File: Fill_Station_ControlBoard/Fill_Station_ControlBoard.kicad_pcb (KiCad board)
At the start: 4 copper layers, 161 parts, among them J10 Screw_Terminal_2_P5.00mm, J3 USB_C_Receptacle_USB2.0_14P, J4 Conn_02x05_Counter_Clockwise, J5 436500200, J6 RJ45_Wuerth_7499010211A, J7 436500200, J8 DE9_Socket_MountingHoles, J9 436500200, SW1 CK_KMS2xxG, U1 STM32H747IITx, U2 USBLC6-2SC6, U3 TCAN337G, U4 TPS2116DRL, U5 LAN8742A, U7 OKI-78SR-5_1.5-W36-C, Y1 ASV-32.768kHz, Y1 Crystal 25MHz, Y2 Crystal 32.768 kHz, Y3 ASV-25.000MHz

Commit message: début layout
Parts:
- removed the C26 at (128.3, 82.5)
- removed the C27 at (128.3, 85.0)
- removed the C33 at (130.6, 72.5)
- removed the C34 at (130.6, 75.0)
- removed C79, C80, C81, C82, C84, C85: C, Capacitor_SMD:C_0603_1608Metric
- removed R89, R90: R_US, Resistor_SMD:R_0603_1608Metric
- removed the Y1 at (134.4, 84.4)
- removed the Y2 at (136.1, 73.8)
- added C10: 47uF, Capacitor_SMD:CP_Elec_4x5.4, F.Cu at (269.0, 162.6)
- added C11: 47uF, Capacitor_SMD:CP_Elec_4x5.4, F.Cu at (281.8, 162.7)
- added C5: 10u, Capacitor_SMD:C_0603_1608Metric, F.Cu at (223.8, 190.7)
- added C55: 10u, Capacitor_SMD:C_0603_1608Metric, F.Cu at (242.5, 125.3)
- added C56: 0.1u, Capacitor_SMD:C_0603_1608Metric, F.Cu at (242.5, 127.8)
- added C58: 3.3n, Capacitor_SMD:C_0603_1608Metric, F.Cu at (242.5, 130.3)
- added C8: 100n, Capacitor_SMD:C_0603_1608Metric, F.Cu at (223.8, 188.1)
- added CR1: ESDCAN02-2BWY, ESDCAN:SOT323-3L_STM, B.Cu at (185.1, 151.5)
- added D15: 6.4V, Diode_SMD:D_0603_1608Metric, F.Cu at (248.5, 120.0)
- added D4: LED, LED_SMD:LED_0603_1608Metric, F.Cu at (269.0, 156.2)
- added D5: LED, LED_SMD:LED_0603_1608Metric, F.Cu at (285.5, 158.9)
- added F1: Fuse, Fuse:Fuse_0603_1608Metric, F.Cu at (247.1, 165.8)
- added F2: Polyfuse, Fuse:Fuse_0603_1608Metric, F.Cu at (248.5, 122.5)
- added IC1: TPS259573DSGR, Package_SON:WSON-8-1EP_2x2mm_P0.5mm_EP0.9x1.6mm_ThermalVias, F.Cu at (247.2, 157.1)
- added J10: Screw_Terminal_6_P5.00mm, TerminalBlock_Phoenix:TerminalBlock_Phoenix_PT-1,5-6-5.0-H_1x06_P5.00mm_Horizontal, F.Cu at (122.6, 106.8)
- added J11: Micro_SD_Card_Det1, Connector_Card:microSD_HC_Molex_47219-2001, F.Cu at (293.6, 104.7)
- added J2: Ematch1, TerminalBlock_Phoenix:TerminalBlock_Phoenix_PT-1,5-2-5.0-H_1x02_P5.00mm_Horizontal, F.Cu at (270.9, 172.7)
- added J6: Ematch2, TerminalBlock_Phoenix:TerminalBlock_Phoenix_PT-1,5-2-5.0-H_1x02_P5.00mm_Horizontal, F.Cu at (282.5, 172.7)
- added J7: Screw_Terminal_3_P5.00mm, TerminalBlock_Phoenix:TerminalBlock_Phoenix_PT-1,5-3-5.0-H_1x03_P5.00mm_Horizontal, F.Cu at (122.6, 139.1)
- added J8: Screw_Terminal_3_P5.00mm, TerminalBlock_Phoenix:TerminalBlock_Phoenix_PT-1,5-3-5.0-H_1x03_P5.00mm_Horizontal, F.Cu at (132.7, 146.7)
- added J9: Screw_Terminal_3_P5.00mm, TerminalBlock_Phoenix:TerminalBlock_Phoenix_PT-1,5-3-5.0-H_1x03_P5.00mm_Horizontal, F.Cu at (150.0, 146.7)
- added Q1: AO3400A, Package_TO_SOT_SMD:SOT-23, F.Cu at (275.7, 162.6)
- added Q2: AO3400A, Package_TO_SOT_SMD:SOT-23, F.Cu at (288.5, 162.7)
- added R14: 10k, Resistor_SMD:R_0603_1608Metric_Pad0.98x0.95mm_HandSolder, F.Cu at (219.6, 198.2)
- added R16: 10k, Resistor_SMD:R_0603_1608Metric_Pad0.98x0.95mm_HandSolder, F.Cu at (219.6, 195.7)
- added R18: 49.9, Resistor_SMD:R_0603_1608Metric_Pad0.98x0.95mm_HandSolder, F.Cu at (219.6, 188.1)
- added R20: 49.9, Resistor_SMD:R_0603_1608Metric_Pad0.98x0.95mm_HandSolder, F.Cu at (219.6, 190.7)
- added R21: 49.9, Resistor_SMD:R_0603_1608Metric_Pad0.98x0.95mm_HandSolder, F.Cu at (219.6, 193.2)
- added R22: 49.9, Resistor_SMD:R_0603_1608Metric_Pad0.98x0.95mm_HandSolder, F.Cu at (219.6, 200.7)
- added R25: 22, Resistor_SMD:R_0603_1608Metric_Pad0.98x0.95mm_HandSolder, F.Cu at (297.2, 162.6)
- added R26: 10k, Resistor_SMD:R_0603_1608Metric_Pad0.98x0.95mm_HandSolder, F.Cu at (297.2, 152.5)
- added R27: 50k, Resistor_SMD:R_0603_1608Metric_Pad0.98x0.95mm_HandSolder, F.Cu at (297.2, 157.5)
- added R28: 10k, Resistor_SMD:R_0603_1608Metric_Pad0.98x0.95mm_HandSolder, F.Cu at (297.2, 155.0)
- added R31: *, Resistor_SMD:R_0603_1608Metric_Pad0.98x0.95mm_HandSolder, F.Cu at (297.2, 160.1)
- added R33: *, Resistor_SMD:R_0603_1608Metric_Pad0.98x0.95mm_HandSolder, F.Cu at (297.2, 175.1)
- added R34: 22, Resistor_SMD:R_0603_1608Metric_Pad0.98x0.95mm_HandSolder, F.Cu at (297.2, 165.1)
- added R35: 10k, Resistor_SMD:R_0603_1608Metric_Pad0.98x0.95mm_HandSolder, F.Cu at (297.2, 167.6)
- added R36: 50k, Resistor_SMD:R_0603_1608Metric_Pad0.98x0.95mm_HandSolder, F.Cu at (297.2, 170.1)
- added R37: 10k, Resistor_SMD:R_0603_1608Metric_Pad0.98x0.95mm_HandSolder, F.Cu at (297.2, 172.6)
- added R38: 22, Resistor_SMD:R_0402_1005Metric, F.Cu at (225.8, 79.9)
- added R39: 22, Resistor_SMD:R_0402_1005Metric, F.Cu at (235.7, 89.6)
- added R40: 22, Resistor_SMD:R_0402_1005Metric, F.Cu at (224.8, 79.9)
- added R41: 22, Resistor_SMD:R_0402_1005Metric, F.Cu at (223.8, 79.9)
- added R42: 22, Resistor_SMD:R_0402_1005Metric, F.Cu at (235.7, 88.6)
- added R43: 10k, Resistor_SMD:R_0402_1005Metric, F.Cu at (275.5, 98.9)
- added R44: 10k, Resistor_SMD:R_0402_1005Metric, F.Cu at (276.7, 98.9)
- added R45: 10k, Resistor_SMD:R_0402_1005Metric, F.Cu at (277.9, 98.9)
- added R46: 10k, Resistor_SMD:R_0402_1005Metric, F.Cu at (279.1, 98.9)
- added R47: 10k, Resistor_SMD:R_0402_1005Metric, F.Cu at (280.3, 98.9)
- added R48: 10k, Resistor_SMD:R_0402_1005Metric, F.Cu at (281.4, 98.9)
- added R59: 100k, Resistor_SMD:R_0805_2012Metric, F.Cu at (238.3, 125.5)
- added R60: *, Resistor_SMD:R_0805_2012Metric, F.Cu at (238.3, 128.4)
- added R61: *, Resistor_SMD:R_0805_2012Metric, F.Cu at (238.3, 131.4)
- added U4: TPS62130, Package_DFN_QFN:VQFN-16-1EP_3x3mm_P0.5mm_EP1.68x1.68mm_ThermalVias, F.Cu at (239.1, 121.3)
- C6: renamed from C28; value ~ -> 10u
- C60: renamed from C37; moved to B.Cu
- C61: renamed from C83; value C -> 22u
- C62: renamed from C38; moved to B.Cu
- C7: renamed from C29; value ~ -> 100n
- R1: renamed from R24; value 33 -> 22
- R17: renamed from R37; value 270 -> 10k
- R2: value 33 -> 22
- R3: renamed from R36; value 33 -> 22
- R4: renamed from R21; value 33 -> 22
- R52: renamed from R38; footprint Resistor_SMD:R_0603_1608Metric_Pad0.98x0.95mm_HandSolder -> Capacitor_SMD:C_0402_1005Metric
- R54: renamed from R47; footprint Resistor_SMD:R_0603_1608Metric_Pad0.98x0.95mm_HandSolder -> Capacitor_SMD:C_0402_1005Metric
- R6: renamed from R22; value 33 -> 22
- R65: renamed from R15; footprint Resistor_SMD:R_0805_2012Metric -> Capacitor_SMD:C_0603_1608Metric
- R66: renamed from R16; footprint Resistor_SMD:R_0805_2012Metric -> Capacitor_SMD:C_0603_1608Metric
- R7: renamed from R25; value 33 -> 22
- R75: renamed from R29; footprint Resistor_SMD:R_0805_2012Metric -> Capacitor_SMD:C_0603_1608Metric
- R8: renamed from R23; value 33 -> 22
- moved C64 341.9 mm to (245.1, 157.1), turned to 90 degrees
- moved U3 338.5 mm to (255.0, 148.8), turned to 90 degrees
- moved C57 336.2 mm to (253.3, 172.3)
- moved R78 335.2 mm to (248.4, 153.8)
- moved R67 333.7 mm to (243.3, 160.1), turned to 180 degrees
- moved R77 333.2 mm to (245.1, 153.5), turned to 90 degrees
- moved R73 331.8 mm to (252.1, 157.1), turned to 90 degrees
- moved R68 330.9 mm to (242.6, 157.8), turned to 90 degrees
- moved C59 329.6 mm to (253.4, 164.2)
- moved C61 329.0 mm to (247.5, 130.4)
- moved C12 328.3 mm to (278.7, 106.1)
- moved C13 328.3 mm to (278.7, 108.6)
- moved D6 327.7 mm to (240.0, 164.5), turned to 180 degrees
- moved J13 325.6 mm to (242.1, 172.4)
- moved R66 317.1 mm to (259.1, 136.2), turned to 90 degrees
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- renumbered C12 to C1, C45 to C12, C46 to C13, C6 to C15, C48 to C16, C31 to C17, C25 to C18, C24 to C19, C9 to C2, C32 to C20, C23 to C21, C42 to C22, C43 to C23, C44 to C24, C55 to C25, C2 to C26, C3 to C27, C56 to C28, C4 to C29, C10 to C3, C1 to C30, C5 to C31, C19 to C32, C8 to C33, C20 to C34, C14 to C35, C57 to C36, C15 to C37, C21 to C38, C16 to C39, C13 to C4, C22 to C40, C17 to C41, C36 to C42, C18 to C43, C54 to C44, C50 to C45, C7 to C46, C49 to C47, C33 to C48, C26 to C49, C11 to C50, C27 to C51, C34 to C52, C40 to C53, C41 to C54, C52 to C57, C53 to C59, C60 to C64, C35 to C66, C51 to C9, D12 to D1, D6 to D10, D5 to D11, D7 to D12, D8 to D13, D9 to D14, D11 to D2, D10 to D3, D13 to D6, D2 to D7, D4 to D8, D1 to D9, J6 to J1, J4 to J12, J10 to J13, J8 to J14, J3 to J15, J7 to J3, J9 to J4, R32 to R10, R33 to R11, R26 to R12, R17 to R13, R30 to R15, R8 to R19, R18 to R23, R19 to R24, R1 to R29, R9 to R30, R20 to R32, R27 to R49, R28 to R5, R14 to R50, R39 to R51, R48 to R53, R42 to R55, R43 to R56, R46 to R57, R5 to R58, R44 to R62, R53 to R63, R54 to R64, R51 to R67, R52 to R68, R34 to R69, R35 to R70, R55 to R71, R40 to R72, R69 to R73, R41 to R74, R45 to R76, R67 to R77, R68 to R78, R3 to R79, R4 to R80, R13 to R81, R12 to R82, R31 to R9, U5 to U1, U1 to U2, U7 to U3, U3 to U5, U4 to U6, U2 to U7, Y3 to Y1, Y1 to Y2
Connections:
- net Net-(J3-D+-PadA6) renamed /USB/D+
- net Net-(J3-D--PadA7) renamed /USB/D-
- net Net-(J5-Pad1) renamed /Control/Servo1
- net Net-(J7-Pad1) renamed /Control/Servo2
- net Net-(J9-Pad1) renamed /Control/Servo3
- C6 pad 1: Net-(U5-VDD1A) -> 3V3A
- C7 pad 1: Net-(U5-VDD1A) -> 3V3A
- C9 pad 1: 3V3 -> 3V3A
- J1 pad 4: 3V3 -> 3V3A
- J1 pad 5: 3V3 -> 3V3A
- J1 pad 8: CHASSIS -> unconnected-(J1-Pad8)
- U1 pad 1: Net-(U5-VDD1A) -> 3V3A
- U1 pad 19: Net-(U5-VDD1A) -> 3V3A
- U1 pad 5: unconnected-(U5-XTAL1/CLKIN-Pad5) -> /MCU/Clock_25Mhz
- U6 pad 5: unconnected-(U4-MODE-Pad5) -> 5V_BAT
- U7 pad 5: +5V -> 5V_USB
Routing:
- net /CAN FD/CAN_P: track 0.00 -> 20.7 mm, vias 0 -> 1
- net /CAN FD/CAN_N: track 0.00 -> 16.2 mm, vias 0 -> 1
- net GND: track 0.00 -> 13.5 mm, vias 0 -> 7
- net Net-(IC1-~{EN}/OVLO): track 0.00 -> 6.33 mm
- net Net-(F1-Pad1): track 0.00 -> 5.81 mm
- net 3V3: track 0.00 -> 4.59 mm, vias 0 -> 1
- net Net-(U5-S): track 0.00 -> 3.57 mm
- net Net-(U5-RXD): track 0.00 -> 3.38 mm
- net Net-(U5-TXD): track 0.00 -> 3.38 mm
- net Net-(U6-PR1): track 0.00 -> 3.36 mm
- net Net-(IC1-ILM): track 0.00 -> 2.86 mm
- net 5V: track 0.00 -> 2.55 mm
- net 5V_BAT: track 0.00 -> 2.49 mm
- net /CAN FD/CAN.FAULT: track 0.00 -> 2.24 mm
- net Net-(U6-ST): track 0.00 -> 2.15 mm
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- added copper zone on F.Cu, net 12.8V
- added copper zone on F.Cu, net 12.8V_BAT
- added copper zone on In2.Cu, net 3V3
- added copper zone on F.Cu, net 5V
- added copper zone on F.Cu, net 5V_BAT
- added copper zone on F.Cu, net 5V_USB
- added copper zone on In1.Cu, net GND

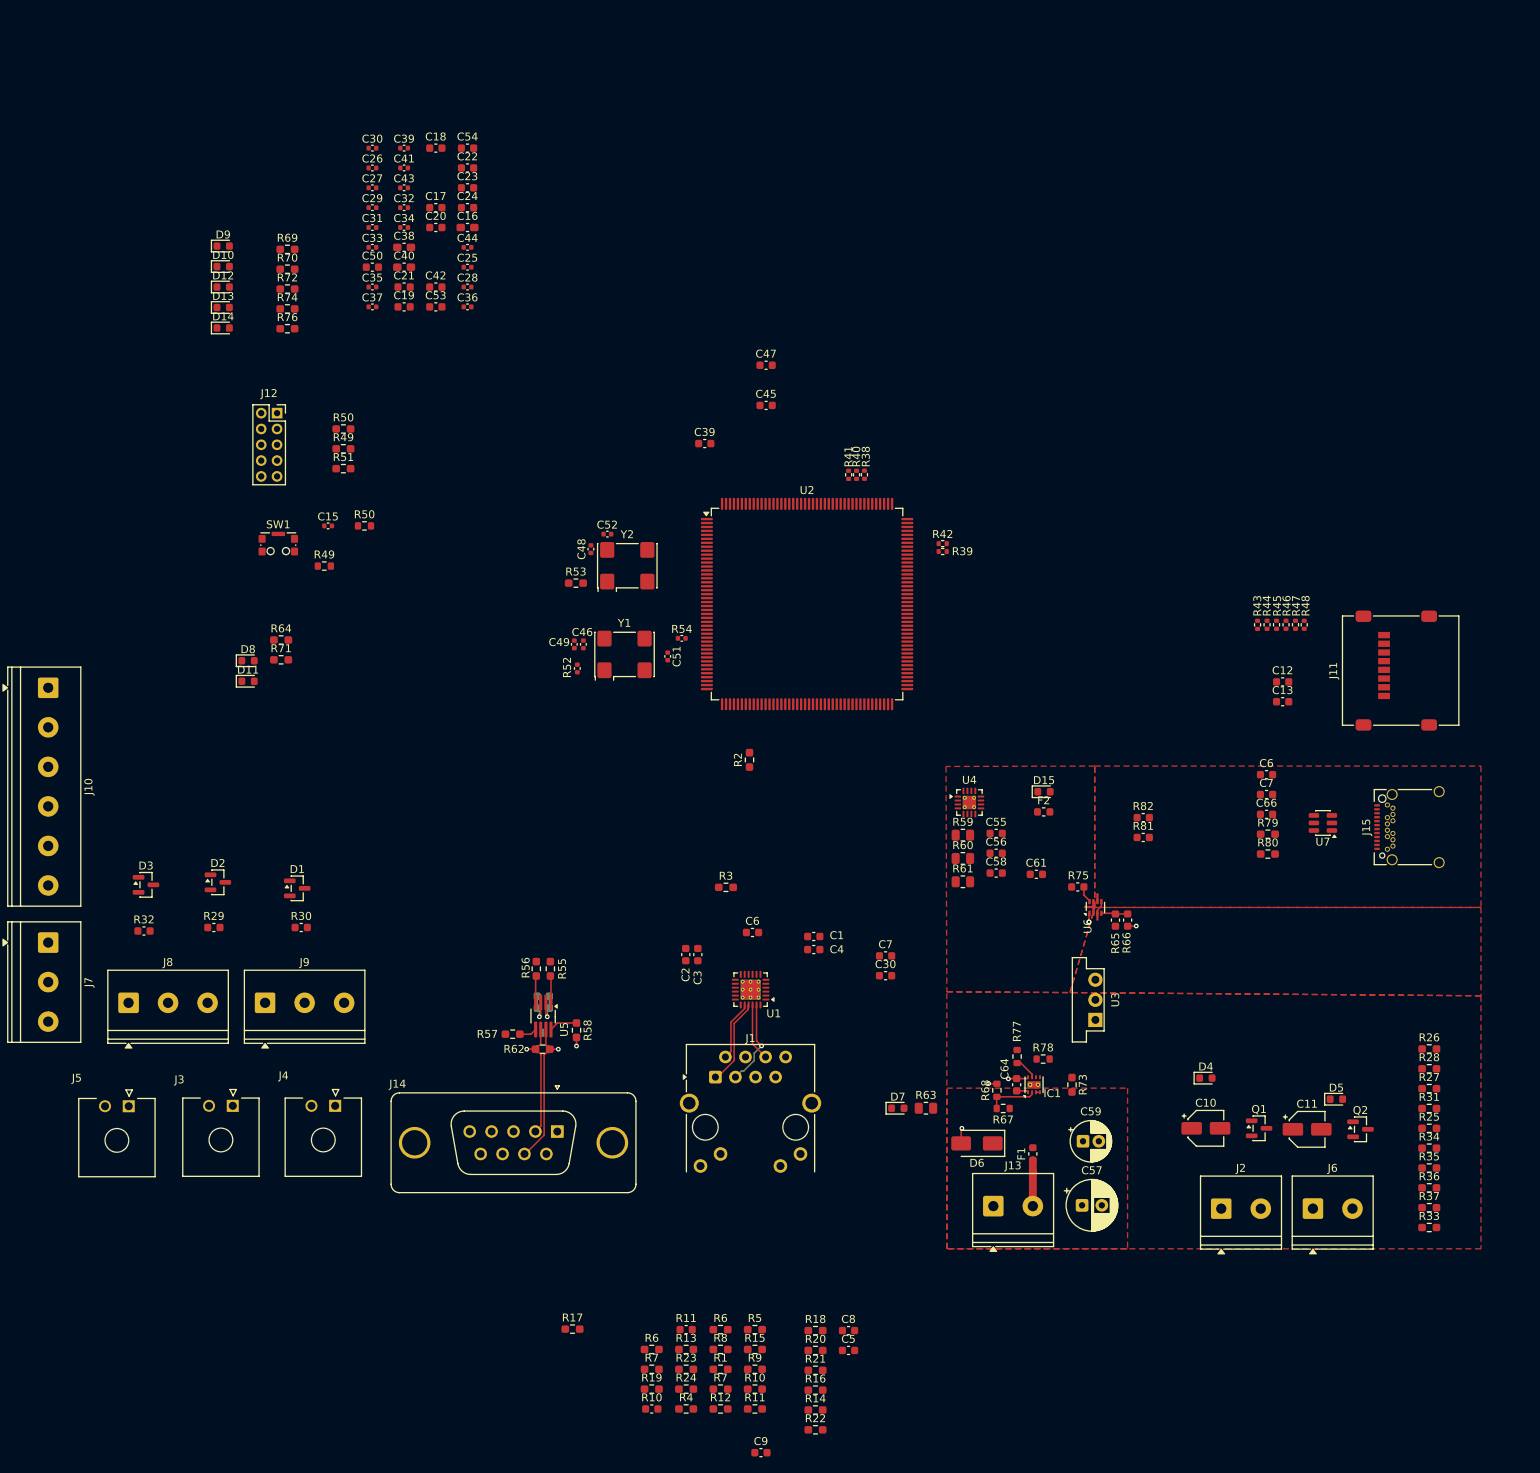
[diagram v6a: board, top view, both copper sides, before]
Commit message: wiring de certaines parties du PCB et placement de quelques composantes sur le PCB
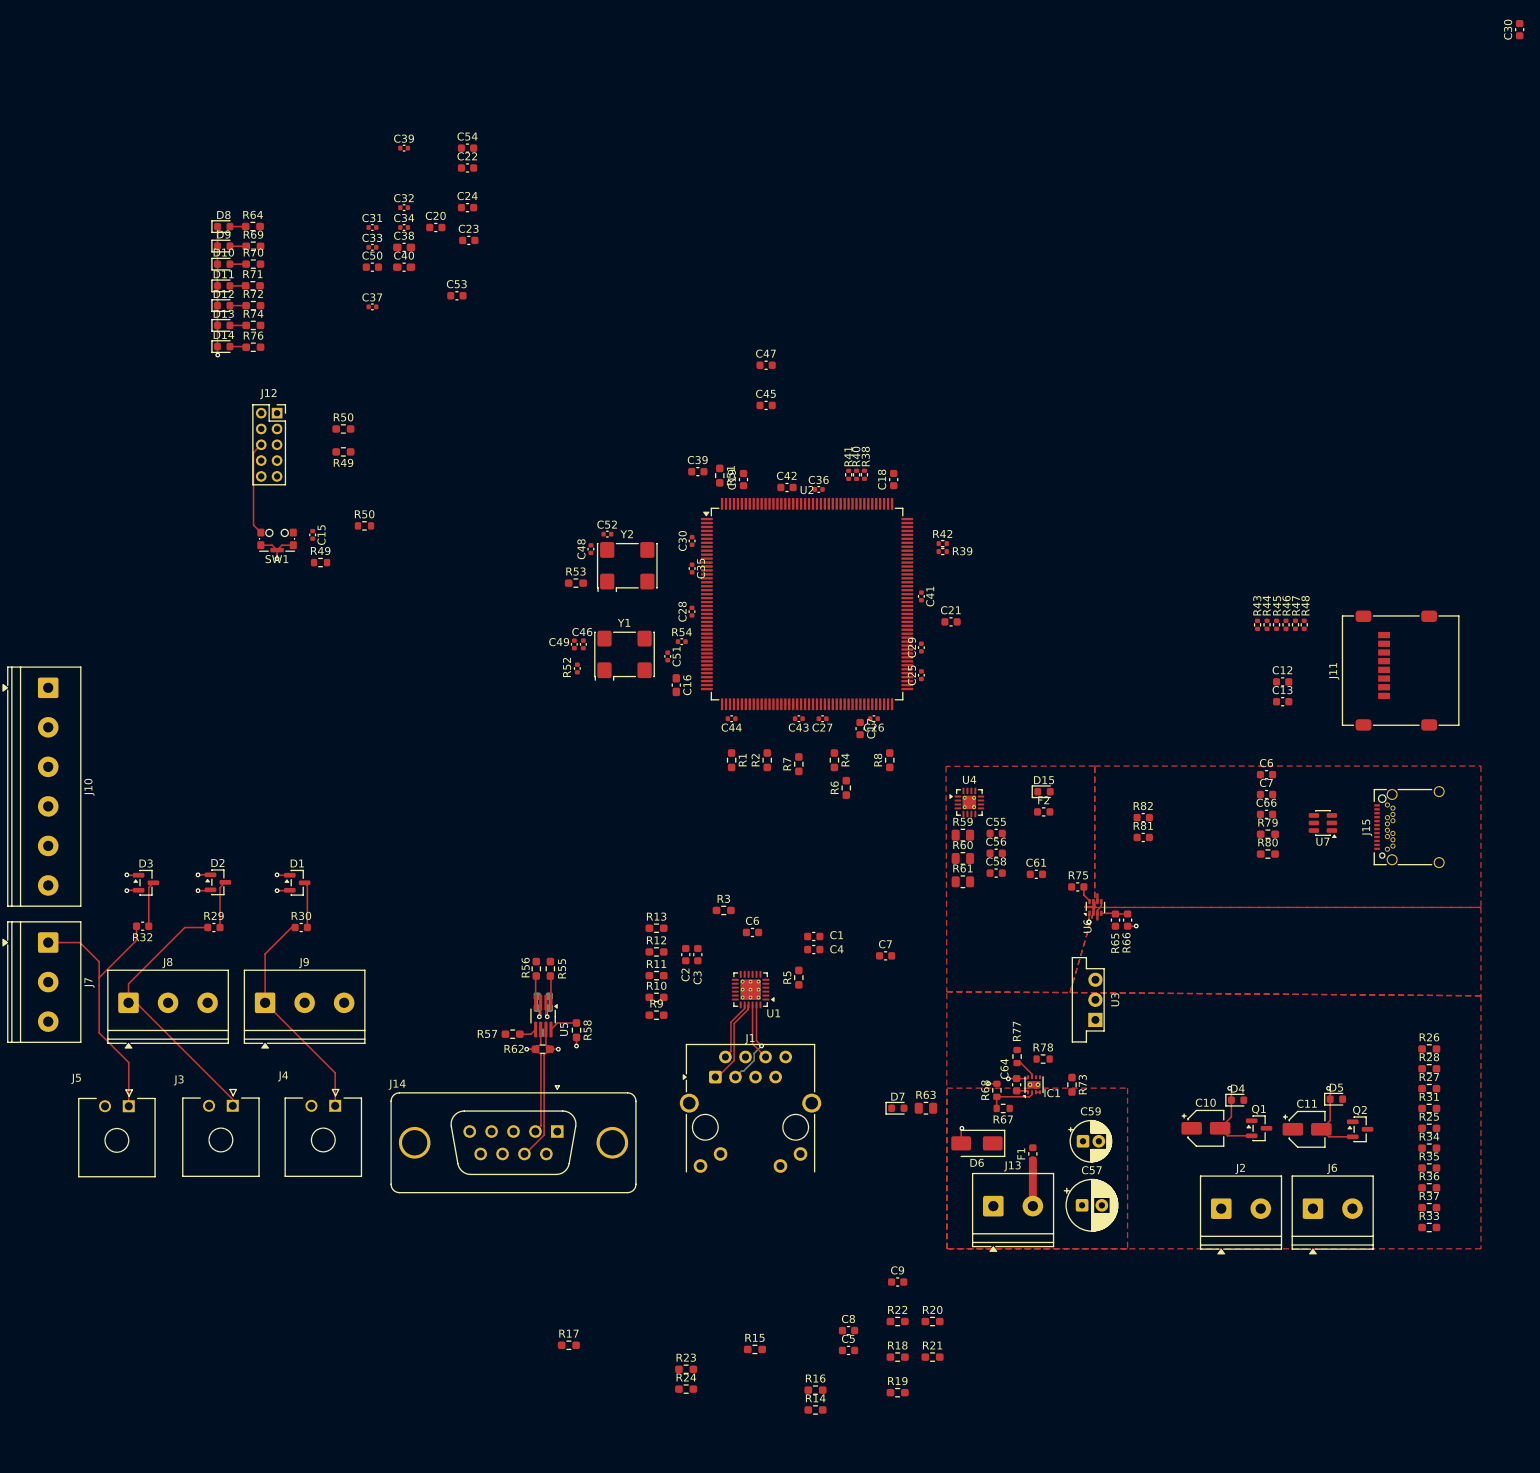
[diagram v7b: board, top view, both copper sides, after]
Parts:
- removed the R10 at (198.9, 198.1)
- removed the R11 at (203.2, 188.0)
- removed the R6 at (198.9, 190.5)
- removed the R7 at (198.9, 193.0)
- moved C30 144.1 mm to (308.7, 23.6), turned to 90 degrees
- moved C26 94.2 mm to (227.0, 110.8), turned to 180 degrees
- moved C29 89.0 mm to (233.0, 101.8), turned to 90 degrees
- moved C27 88.0 mm to (220.5, 110.8), turned to 180 degrees
- moved C17 85.0 mm to (225.2, 112.0), turned to -90 degrees
- moved C41 85.0 mm to (233.0, 95.3), turned to -90 degrees
- moved R4 84.2 mm to (222.0, 116.0), turned to -90 degrees
- moved C43 83.7 mm to (217.5, 110.8), turned to 180 degrees
- moved C21 81.1 mm to (236.8, 98.5)
- moved R7 79.7 mm to (217.5, 116.5), turned to 90 degrees
- moved R8 77.5 mm to (229.0, 116.0), turned to 90 degrees
- moved C25 77.2 mm to (233.0, 105.2), turned to 90 degrees
- moved R1 77.1 mm to (209.0, 116.0), turned to -90 degrees
- moved C18 71.5 mm to (229.5, 80.5), turned to 90 degrees
- moved R6 70.3 mm to (223.5, 119.5), turned to 90 degrees
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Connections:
- C25 pad 2: Net-(C25-Pad2) -> GND
- C28 pad 2: Net-(C25-Pad2) -> GND
- C30 pad 2: Net-(C25-Pad2) -> GND
- C32 pad 2: Net-(C25-Pad2) -> GND
- C34 pad 2: Net-(C25-Pad2) -> GND
- C36 pad 2: Net-(C25-Pad2) -> GND
- C38 pad 2: Net-(C25-Pad2) -> GND
- C40 pad 2: Net-(C25-Pad2) -> GND
- C42 pad 2: Net-(C25-Pad2) -> GND
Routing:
- net GND: track 13.5 -> 59.9 mm, vias 7 -> 14
- net /Control/Servo1: track 0.00 -> 35.7 mm
- net /Control/Servo2: track 0.00 -> 34.4 mm
- net /Control/Servo3: track 0.00 -> 28.1 mm
- net /MCU/NRST: track 0.00 -> 11.9 mm
- net /Control/Servo.Signal2: track 0.00 -> 5.99 mm
- net /Control/Servo.Signal3: track 0.00 -> 5.80 mm
- net /Control/Servo.Signal1: track 0.00 -> 5.74 mm
- net 3V3: track 4.59 -> 9.36 mm, vias 1 -> 4
- net Net-(D14-A): track 0.00 -> 2.22 mm
- net Net-(D9-A): track 0.00 -> 2.06 mm
- net Net-(D12-A): track 0.00 -> 2.05 mm
- net Net-(D13-A): track 0.00 -> 2.05 mm
- net Net-(D10-A): track 0.00 -> 2.05 mm
- net Net-(D8-A): track 0.00 -> 1.99 mm
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
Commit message: Petits changements et truc que j'ai fait lundi
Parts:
- removed the R49 at (157.0, 91.0)
- moved C34 78.0 mm to (233.2, 90.8)
- moved C40 53.4 mm to (202.8, 93.8), turned to 180 degrees
- moved C24 47.9 mm to (209.0, 80.5), turned to 90 degrees
- moved R9 15.8 mm to (211.5, 138.0)
- moved R49 13.1 mm to (147.0, 74.8), turned to -90 degrees
- moved C2 12.4 mm to (215.5, 141.8), turned to 0 degrees
- moved C3 11.2 mm to (215.5, 143.5), turned to 0 degrees
- moved C6 11.1 mm to (217.8, 147.0)
- moved C38 7.42 mm to (171.8, 45.0)
- moved C23 6.66 mm to (181.2, 46.5)
- moved R5 6.25 mm to (223.8, 143.2)
- moved C52 5.37 mm to (190.5, 92.0)
- moved C16 2.66 mm to (203.8, 104.5), turned to 90 degrees
- moved R54 2.21 mm to (200.5, 100.8)
- moved C49 1.88 mm to (190.0, 103.0), turned to 0 degrees
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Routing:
- net GND: track 59.9 -> 125.4 mm, vias 14 -> 26
- net 3V3: track 9.36 -> 60.9 mm, vias 4 -> 16
- net Net-(Y2-EN): track 0.00 -> 5.60 mm
- net /MCU/NRST: track 11.9 -> 17.3 mm
- net 3V3A: track 0.00 -> 4.74 mm
- net Net-(Y1-EN): track 0.00 -> 4.67 mm
- net Net-(Y1-OUT): track 0.00 -> 2.08 mm
- net /MCU/Clock_25Mhz: track 0.00 -> 1.97 mm
